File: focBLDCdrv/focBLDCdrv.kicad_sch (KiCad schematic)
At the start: 19 parts, among them J1 Screw_Terminal_01x02, J2 Screw_Terminal_01x03, J5 Conn_02x03_Counter_Clockwise, J6 Conn_01x03, U1 MFC8316A

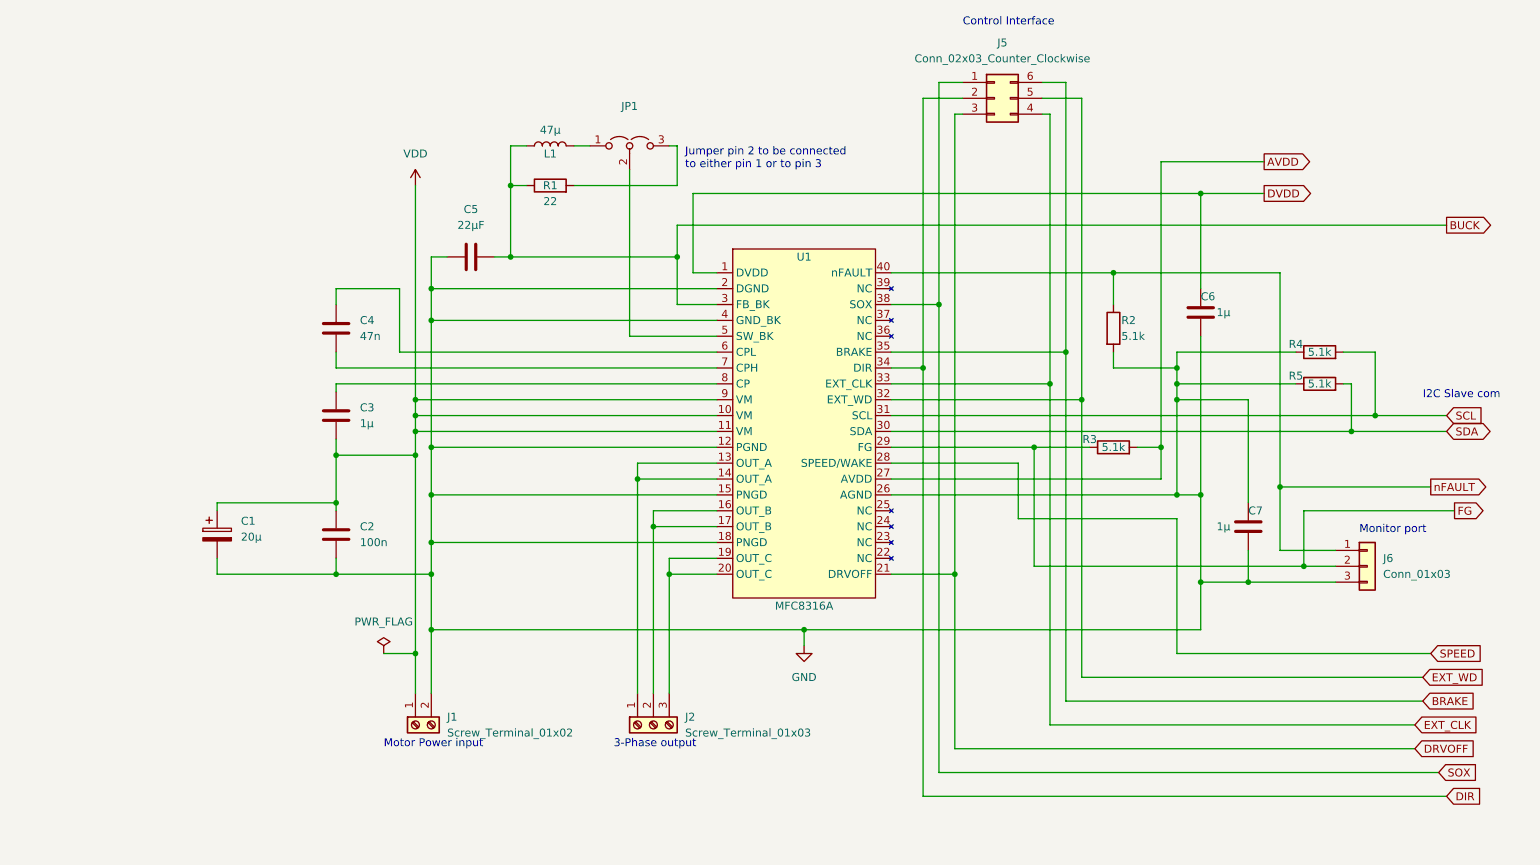
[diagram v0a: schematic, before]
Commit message: J4 header orientation changed, mount holes added and additinal AGND fill
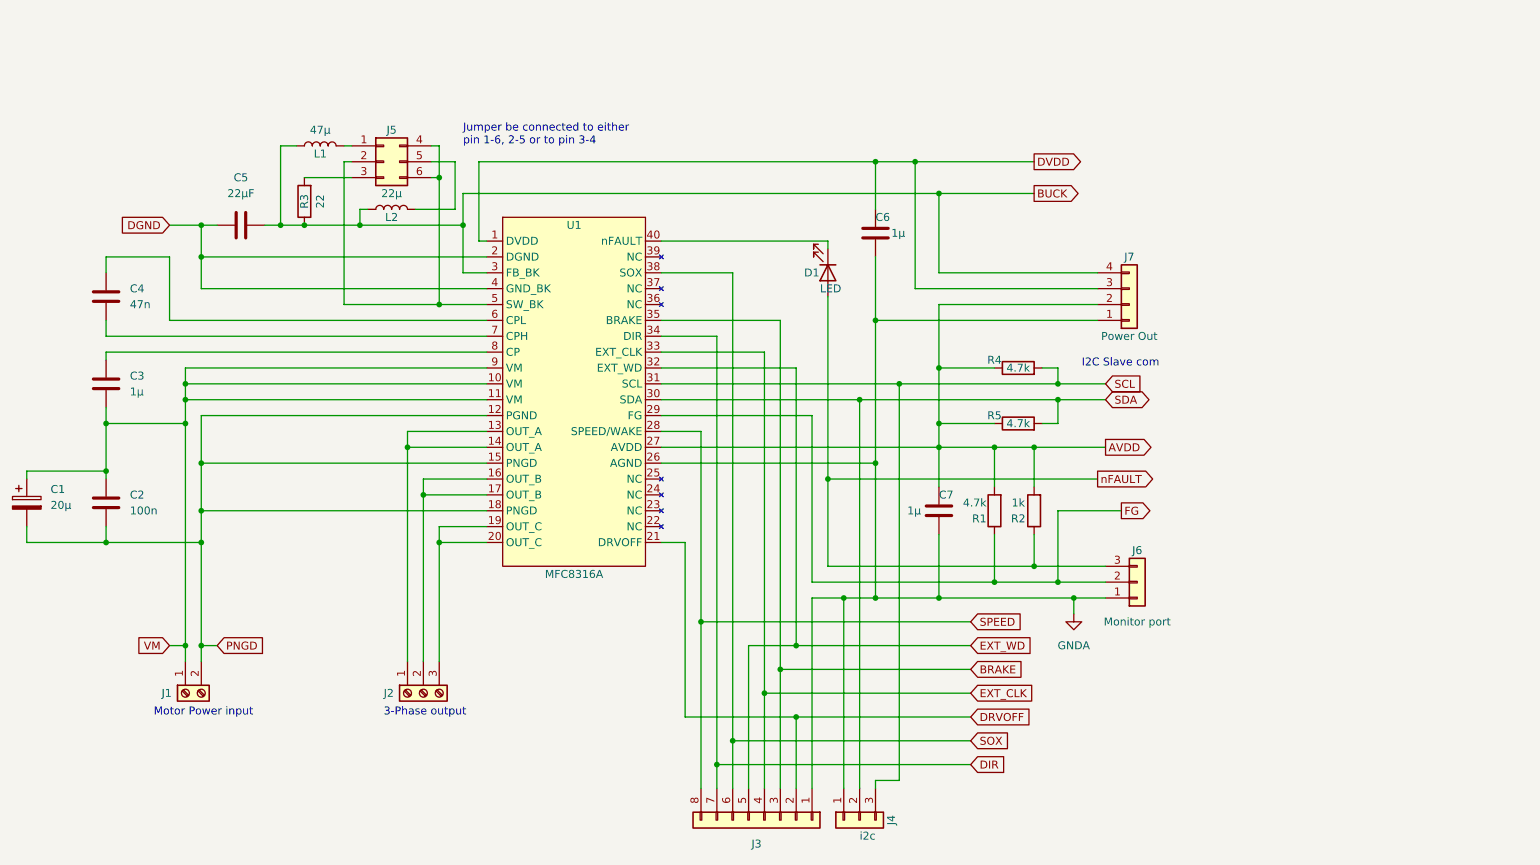
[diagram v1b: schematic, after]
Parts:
- removed J5: Conn_02x03_Counter_Clockwise, Connector_PinHeader_2.54mm:PinHeader_2x03_P2.54mm_Vertical_SMD, symbol Connector_Generic:Conn_02x03_Counter_Clockwise
- removed JP1: (no value), symbol Jumper:Jumper_3_Open
- added D1: LED, LED_SMD:LED_1206_3216Metric_Pad1.42x1.75mm_HandSolder, symbol Device:LED
- added J3: Conn_01x08, Connector_PinHeader_2.54mm:PinHeader_1x08_P2.54mm_Vertical, symbol Connector_Generic:Conn_01x08
- added J4: i2c, Connector_PinHeader_2.54mm:PinHeader_1x03_P2.54mm_Vertical, symbol Connector_Generic:Conn_01x03
- added J5: Conn_02x03_Top_Bottom, Connector_PinHeader_2.54mm:PinHeader_2x03_P2.54mm_Vertical, symbol Connector_Generic:Conn_02x03_Top_Bottom
- added J7: Power Out, Connector_PinHeader_2.54mm:PinHeader_1x04_P2.54mm_Vertical, symbol Connector_Generic:Conn_01x04
- added L2: 22µ, Inductor_SMD:L_1206_3216Metric, symbol Device:L
- C2, C3, C4, C6, C7: footprint Capacitor_SMD:C_1206_3216Metric_Pad1.33x1.80mm_HandSolder -> Capacitor_SMD:C_0805_2012Metric_Pad1.18x1.45mm_HandSolder
- J6: value Conn_01x03 -> Monitor port
- R1: value 22 -> 4.7k; footprint Resistor_SMD:R_1206_3216Metric_Pad1.30x1.75mm_HandSolder -> Resistor_SMD:R_0805_2012Metric_Pad1.20x1.40mm_HandSolder
- R2: value 5.1k -> 1k; footprint Resistor_SMD:R_1206_3216Metric_Pad1.30x1.75mm_HandSolder -> Resistor_SMD:R_0805_2012Metric_Pad1.20x1.40mm_HandSolder
- R3: value 5.1k -> 22
- R4, R5: value 5.1k -> 4.7k; footprint Resistor_SMD:R_1206_3216Metric_Pad1.30x1.75mm_HandSolder -> Resistor_SMD:R_0805_2012Metric_Pad1.20x1.40mm_HandSolder
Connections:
- net AVDD: now also C7.1, R1.2, R2.2, R4.1, R5.1, J7.2 (Pin_2); no longer R3.2
- net BRAKE: now also J3.3 (Pin_3)
- net BUCK: now also R3.1, J7.4 (Pin_4), L2.1; no longer R1.1
- net DIR: now also J3.7 (Pin_7)
- net DRVOFF: now also J3.2 (Pin_2)
- net DVDD: now also J7.3 (Pin_3)
- net EXT_CLK: now also J3.4 (Pin_4)
- net EXT_WD: now also J3.5 (Pin_5)
- net FG: now also R1.1; no longer R3.1
- net SCL: now also J4.3 (Pin_3)
- net SDA: now also J4.2 (Pin_2)
- net SOX: now also J3.6 (Pin_6)
- net SPEED: now also J3.8 (Pin_8)
- net nFAULT: now also J6.3 (Pin_3), D1.2 (A); no longer J6.1 (Pin_1), U1.40 (nFAULT)
- net at U1.5 (SW_BK): now also J5.2 (Pin_2), J5.4 (Pin_4), J5.6 (Pin_6)
- net at L1.2: now also J5.1 (Pin_1)
- removed net GND: C1.2, C2.2, C5.1, C6.2, C7.1, C7.2, J1.2 (Pin_2), J6.3 (Pin_3), R2.2, R4.1, R5.1, U1.12 (PGND), U1.15 (PNGD), U1.18 (PNGD), U1.2 (DGND), U1.26 (AGND), U1.4 (GND_BK)
- net VDD renamed VM
- new net: J5.3 (Pin_3), R3.2
- new net: J5.5 (Pin_5), L2.2
- new net: D1.1 (K), U1.40 (nFAULT)
- new net DGND: C5.1, U1.2 (DGND), U1.4 (GND_BK)
- new net GNDA: C6.2, C7.2, J3.1 (Pin_1), J4.1 (Pin_1), J6.1 (Pin_1), J7.1 (Pin_1), U1.26 (AGND)
- new net PNGD: C1.2, C2.2, J1.2 (Pin_2), U1.12 (PGND), U1.15 (PNGD), U1.18 (PNGD)
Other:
- note added: "Jumper be connected to either pin 1-6, 2-5 or to pin 3-4"
- note removed: "Control Interface"
- note removed: "Jumper pin 2 to be connected to either pin 1 or to pin 3"
- note removed: "Monitor port"
- moved on the sheet: C1, C2, C3, C4, C5, C6, J1, J2, J6, R4, R5, U1
